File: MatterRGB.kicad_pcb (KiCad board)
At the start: 4 copper layers, 24 x 35 mm, 49 parts, among them J1 USB4105, J2 S4B-PH-K-S, J4 S2B-XH-A-1, J5 S2B-PH-K-S, SW1 NO, SW2 NO, U1 FUSB302B01MPX, U2 ESP32-S3-WROOM-1-N8R8, U3 DRV8955, U5 LMR50410Y3FQDBVRQ1

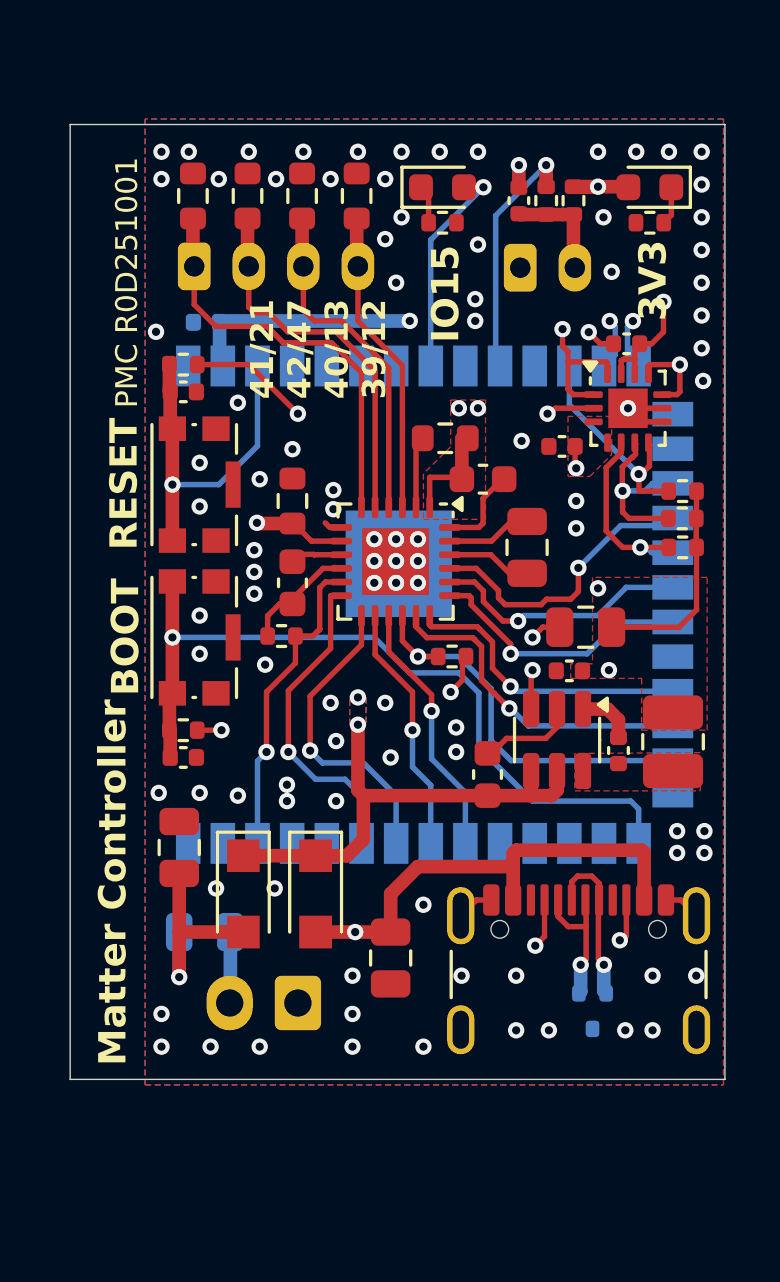
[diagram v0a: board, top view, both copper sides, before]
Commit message: Added new connector/mounting strategy
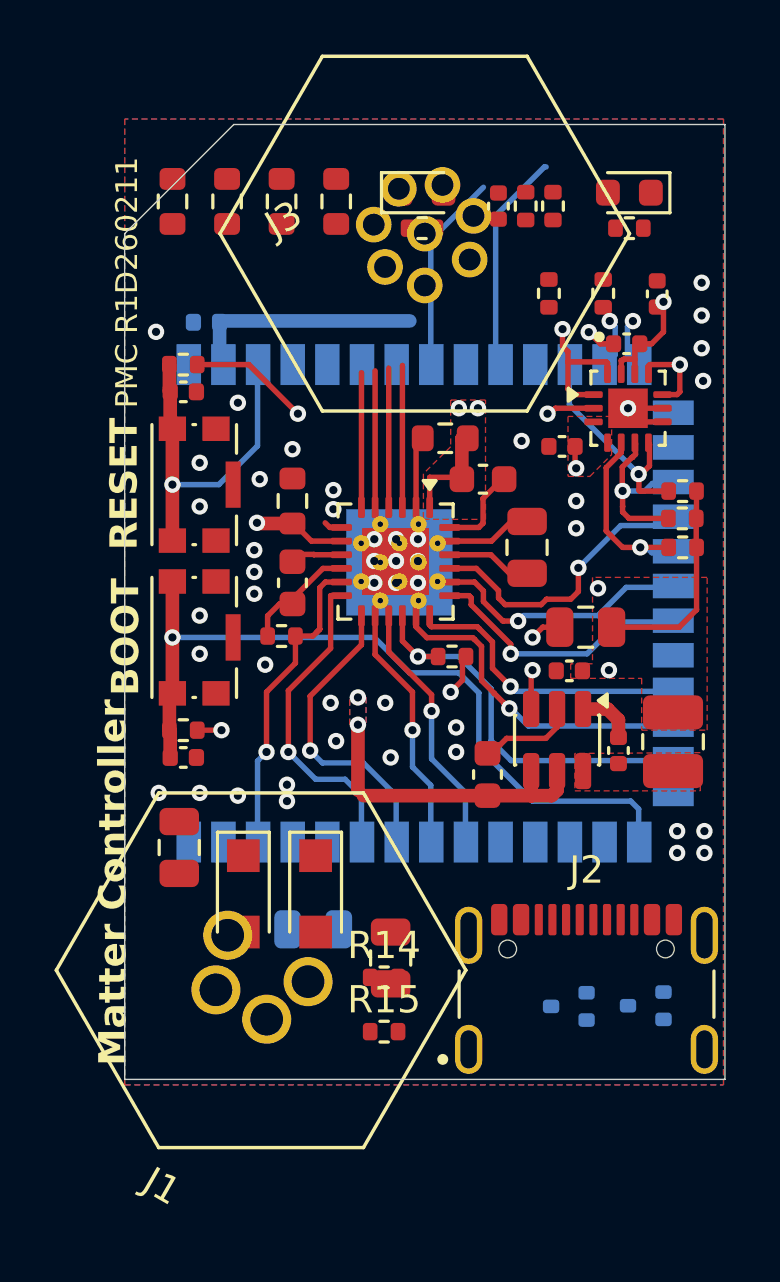
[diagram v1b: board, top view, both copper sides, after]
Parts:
- removed J4: S2B-XH-A-1, Connector_JST:JST_XH_S2B-XH-A-1_1x02_P2.50mm_Horizontal
- removed J5: S2B-PH-K-S, Connector_JST:JST_PH_S2B-PH-K_1x02_P2.00mm_Horizontal
- added C18: 100n, Capacitor_SMD:C_0402_1005Metric, F.Cu at (116.8, 86.2)
- added D4: RCLAMP0582B.TCT, Package_TO_SOT_SMD:SOT-416, B.Cu at (113.5, 112.3)
- added J3: CDM805-08A-FP-F011-67, PCM_PartyWagon112_Connector_M8:CUI_CDM805-08A-FP-F011-67, F.Cu at (108.2, 84.0)
- added R12: 10k, Resistor_SMD:R_0402_1005Metric, F.Cu at (112.8, 86.2)
- added R13: 10k, Resistor_SMD:R_0402_1005Metric, F.Cu at (114.8, 86.2)
- added R14: 0, Resistor_SMD:R_0402_1005Metric, F.Cu at (106.8, 111.3)
- added R15: 0, Resistor_SMD:R_0402_1005Metric, F.Cu at (106.8, 113.2)
- J1: value USB4105 -> CDM806-04A-MP-F011-67; footprint Connector_USB:USB_C_Receptacle_GCT_USB4105-xx-A_16P_TopMnt_Horizontal -> PCM_PartyWagon112_Connector_M8:CUI_CDM806-04A-MP-F011-67
- J2: value S4B-PH-K-S -> USB4105; footprint Connector_JST:JST_PH_S4B-PH-K_1x04_P2.00mm_Horizontal -> Connector_USB:USB_C_Receptacle_GCT_USB4105-xx-A_16P_TopMnt_Horizontal; moved to F.Cu
- U2: value ESP32-S3-WROOM-1-N8R8 -> ESP32-S3-WROOM-1U-N8R8; footprint RF_Module:ESP32-S3-WROOM-1 -> RF_Module:ESP32-S3-WROOM-1U
- U5: value LMR50410Y3FQDBVRQ1 -> LMR51610YFDBVR
- moved J2 31.1 mm to (114.2, 112.8)
- moved J1 11.7 mm to (102.2, 111.0), turned to 150 degrees
- moved F1 3.98 mm to (104.2, 109.5)
- moved U2 3.17 mm to (108.0, 97.5)
- moved D1 1.96 mm to (116.3, 112.3), turned to 180 degrees
- moved C10 0.78 mm to (103.0, 82.8)
- moved C11 0.78 mm to (99.0, 82.8)
- moved C12 0.78 mm to (101.0, 82.8)
- moved C9 0.78 mm to (105.0, 82.8)
- moved LED1 0.78 mm to (115.8, 82.5)
- moved LED2 0.78 mm to (108.2, 82.5)
- moved R2 0.78 mm to (108.2, 83.8)
- moved R3 0.78 mm to (115.8, 83.8)
- moved C8 0.78 mm to (111.0, 83.0)
- moved R5 0.78 mm to (113.0, 83.0)
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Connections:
- net /IN2 renamed /OUT2_CPU
- net /IN3 renamed /OUT3_CPU
- net /IN4 renamed /OUT4_CPU
- C8 pad 1: Net-(J5-Pin_2) -> /IN0
- F1 pad 2: Net-(J4-Pin_2) -> Net-(J1-Pin_1)
- R1 pad 1: VDD -> +3V3
- R5 pad 2: Net-(J5-Pin_2) -> /IN0
- R6 pad 1: Net-(J5-Pin_2) -> /IN0
- R6 pad 2: /IN0 -> /IN0_MCU
- U2 pad 11: unconnected-(U2-IO18-Pad11) -> /IN1
- U2 pad 20: /IN1 -> /OUT1_CPU
- U3 pad 20: /IN1 -> /OUT1_CPU
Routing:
- net VBUS: track 42.4 -> 24.9 mm, vias 2 -> 1
- net /OUT3: track 15.3 -> 4.94 mm
- net /OUT1_CPU: track 0.00 -> 9.50 mm, vias 0 -> 1
- net /IN1: track 9.50 -> 0.00 mm, vias 1 -> 0
- net /OUT4: track 13.9 -> 5.00 mm
- net Net-(D3-A): track 7.80 -> 0.00 mm, vias 1 -> 0
- net /OUT2: track 12.5 -> 5.10 mm
- net VDC: track 45.5 -> 39.0 mm
- net /OUT1: track 11.3 -> 5.20 mm
- net USB_D+: track 33.4 -> 27.4 mm, vias 2 -> 1
- net USB_D-: track 32.7 -> 27.4 mm, vias 2 -> 1
- net Net-(J5-Pin_2): track 3.98 -> 0.00 mm
- net GND: track 19.0 -> 15.4 mm, vias 98 -> 49
- net +3V3: track 84.7 -> 81.7 mm, vias 9 -> 7
- net Net-(J4-Pin_2): track 2.61 -> 0.00 mm
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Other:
- board size 24 x 35 mm -> 22 x 35 mm
- board text added: "PMC R1D260211"
- board text removed: "3V3"
- board text removed: "41/21 42/47 40/13 39/12"
- board text removed: "IO15"
- board text removed: "PMC R0D251001"
